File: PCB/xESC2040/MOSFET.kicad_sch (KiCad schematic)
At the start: 9 parts, among them J11 Conn_02x02_Counter_Clockwise, Q5 BSC026N08NS5, Q6 BSC026N08NS5

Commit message: WIP new power stage
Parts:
- removed C43: 1nF/100V, Capacitor_SMD:C_0603_1608Metric, symbol Device:C
- removed R43: 33mR, Resistor_SMD:R_2512_6332Metric, symbol Device:R
- removed R44: 10R, Resistor_SMD:R_0603_1608Metric, symbol Device:R
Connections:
- net DRV: now also J11.1 (Pin_1), J11.2 (Pin_2), J11.3 (Pin_3), J11.4 (Pin_4)
- net GND: no longer Q6.1 (S), Q6.2 (S), Q6.3 (S)
- new net MOSFET_GND: Q6.1 (S), Q6.2 (S), Q6.3 (S)
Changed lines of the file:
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@@
   (junction (at 231.14 83.82) (diameter 0) (color 0 0 0 0)
   )
-  (junction (at 218.44 83.82) (diameter 0) (color 0 0 0 0)
-  )
   (junction (at 243.84 86.36) (diameter 0) (color 0 0 0 0)
   )
   (junction (at 176.53 53.34) (diameter 0) (color 0 0 0 0)
   )
-  (junction (at 205.74 83.82) (diameter 0) (color 0 0 0 0)
-  )
   (wire (pts (xy 231.14 83.82) (xy 231.14 86.36))
     (stroke (width 0) (type default) (color 0 0 0 0))
@@
     (stroke (width 0) (type default) (color 0 0 0 0))
   )
-  (wire (pts (xy 218.44 97.79) (xy 218.44 83.82))
-    (stroke (width 0) (type default) (color 0 0 0 0))
-  )
   (wire (pts (xy 190.5 53.34) (xy 176.53 53.34))
     (stroke (width 0) (type default) (color 0 0 0 0))
@@
     (stroke (width 0) (type default) (color 0 0 0 0))
   )
-  (wire (pts (xy 205.74 105.41) (xy 205.74 111.76))
-    (stroke (width 0) (type default) (color 0 0 0 0))
-  )
   (wire (pts (xy 176.53 115.57) (xy 176.53 101.6))
     (stroke (width 0) (type default) (color 0 0 0 0))
@@
     (stroke (width 0) (type default) (color 0 0 0 0))
   )
-  (wire (pts (xy 218.44 105.41) (xy 218.44 115.57))
-    (stroke (width 0) (type default) (color 0 0 0 0))
-  )
   (wire (pts (xy 176.53 83.82) (xy 176.53 91.44))
     (stroke (width 0) (type default) (color 0 0 0 0))
@@
     (stroke (width 0) (type default) (color 0 0 0 0))
   )
-  (wire (pts (xy 205.74 83.82) (xy 218.44 83.82))
-    (stroke (width 0) (type default) (color 0 0 0 0))
-  )
-  (wire (pts (xy 218.44 83.82) (xy 231.14 83.82))
-    (stroke (width 0) (type default) (color 0 0 0 0))
-  )
-  (wire (pts (xy 191.77 83.82) (xy 176.53 83.82))
+  (wire (pts (xy 176.53 83.82) (xy 231.14 83.82))
     (stroke (width 0) (type default) (color 0 0 0 0))
   )
@@
     (stroke (width 0) (type default) (color 0 0 0 0))
   )
-  (wire (pts (xy 205.74 83.82) (xy 205.74 97.79))
-    (stroke (width 0) (type default) (color 0 0 0 0))
-  )
-  (wire (pts (xy 199.39 83.82) (xy 205.74 83.82))
-    (stroke (width 0) (type default) (color 0 0 0 0))
-  )
   (wire (pts (xy 168.91 71.12) (xy 157.48 71.12))
     (stroke (width 0) (type default) (color 0 0 0 0))
   )
+  (hierarchical_label "MOSFET_GND" (shape output) (at 176.53 115.57 270)
+    (effects (font (size 1.27 1.27)) (justify right))
+  )
   (hierarchical_label "DRV" (shape output) (at 135.89 83.82 180)
     (effects (font (size 1.27 1.27)) (justify right))
@@
   )
   (hierarchical_label "LS" (shape input) (at 135.89 96.52 180)
-    (effects (font (size 1.27 1.27)) (justify right))
-  )
-  (hierarchical_label "SENSE" (shape output) (at 205.74 111.76 180)
     (effects (font (size 1.27 1.27)) (justify right))
   )
@@
     (pin "5")
   )
-  (symbol (lib_id "Device:R") (at 195.58 83.82 270)
-    (in_bom yes) (on_board yes)
-    (property "Reference" "R43" (id 0) (at 195.58 78.5622 90))
-    (property "Value" "33mR" (id 1) (at 195.58 80.8736 90))
-    (property "Footprint" "Resistor_SMD:R_2512_6332Metric" (id 2) (at 195.58 82.042 90)
-      (effects (font (size 1.27 1.27)) hide)
-    )
-    (property "Datasheet" "~" (id 3) (at 195.58 83.82 0)
-      (effects (font (size 1.27 1.27)) hide)
-    )
-    (property "LCSC" "C2889925" (id 4) (at 195.58 83.82 0)
-      (effects (font (size 1.27 1.27)) hide)
-    )
-    (property "Stock_PN" "R-2512-.033-3W-5%" (id 5) (at 195.58 83.82 0)
-      (effects (font (size 1.27 1.27)) hide)
-    )
-    (pin "1")
-    (pin "2")
-  )
   (symbol (lib_id "Device:R") (at 153.67 71.12 270)
     (in_bom yes) (on_board yes)
@@
     (pin "2")
   )
-  (symbol (lib_id "Device:R") (at 205.74 101.6 0)
-    (in_bom yes) (on_board yes)
-    (property "Reference" "R44" (id 0) (at 207.518 100.4316 0)
-      (effects (font (size 1.27 1.27)) (justify left))
-    )
-    (property "Value" "10R" (id 1) (at 207.518 102.743 0)
-      (effects (font (size 1.27 1.27)) (justify left))
-    )
-    (property "Footprint" "Resistor_SMD:R_0603_1608Metric" (id 2) (at 203.962 101.6 90)
-      (effects (font (size 1.27 1.27)) hide)
-    )
-    (property "Datasheet" "~" (id 3) (at 205.74 101.6 0)
-      (effects (font (size 1.27 1.27)) hide)
-    )
-    (property "Digikey" "RMCF0603FT10R0CT-ND" (id 4) (at 205.74 101.6 0)
-      (effects (font (size 1.27 1.27)) hide)
-    )
-    (property "Part Number" "RMCF0603FT10R0" (id 5) (at 205.74 101.6 0)
-      (effects (font (size 1.27 1.27)) hide)
-    )
-    (property "Stock_PN" "R-603-10-.1W-1%" (id 6) (at 205.74 101.6 0)
-      (effects (font (size 1.27 1.27)) hide)
-    )
-    (pin "1")
-    (pin "2")
-  )
-  (symbol (lib_id "power:GND") (at 176.53 115.57 0)
-    (in_bom yes) (on_board yes)
-    (property "Reference" "#PWR042" (id 0) (at 176.53 121.92 0)
-      (effects (font (size 1.27 1.27)) hide)
-    )
-    (property "Value" "GND" (id 1) (at 176.657 119.9642 0))
-    (property "Footprint" "" (id 2) (at 176.53 115.57 0)
-      (effects (font (size 1.27 1.27)) hide)
-    )
-    (property "Datasheet" "" (id 3) (at 176.53 115.57 0)
-      (effects (font (size 1.27 1.27)) hide)
-    )
-    (pin "1")
-  )
   (symbol (lib_id "Device:C") (at 190.5 58.42 0)
     (in_bom yes) (on_board yes)
@@
       (effects (font (size 1.27 1.27)) hide)
     )
-    (pin "1")
-  )
-  (symbol (lib_id "Device:C") (at 218.44 101.6 0)
-    (in_bom yes) (on_board yes)
-    (property "Reference" "C43" (id 0) (at 221.361 100.4316 0)
-      (effects (font (size 1.27 1.27)) (justify left))
-    )
-    (property "Value" "1nF/100V" (id 1) (at 221.361 102.743 0)
-      (effects (font (size 1.27 1.27)) (justify left))
-    )
-    (property "Footprint" "Capacitor_SMD:C_0603_1608Metric" (id 2) (at 219.4052 105.41 0)
-      (effects (font (size 1.27 1.27)) hide)
-    )
-    (property "Datasheet" "~" (id 3) (at 218.44 101.6 0)
-      (effects (font (size 1.27 1.27)) hide)
-    )
-    (property "Digikey" "C-603-1000pF-100V-X7R" (id 4) (at 218.44 101.6 0)
-      (effects (font (size 1.27 1.27)) hide)
-    )
-    (property "Part Number" "490-4764-2-ND" (id 5) (at 218.44 101.6 0)
-      (effects (font (size 1.27 1.27)) hide)
-    )
-    (property "Stock_PN" "C-603-1000pF-100V-X7R" (id 6) (at 218.44 101.6 0)
-      (effects (font (size 1.27 1.27)) hide)
-    )
-    (pin "1")
-    (pin "2")
-  )
-  (symbol (lib_id "power:GND") (at 218.44 115.57 0)
-    (in_bom yes) (on_board yes)
-    (property "Reference" "#PWR044" (id 0) (at 218.44 121.92 0)
-      (effects (font (size 1.27 1.27)) hide)
-    )
-    (property "Value" "GND" (id 1) (at 218.567 119.9642 0))
-    (property "Footprint" "" (id 2) (at 218.44 115.57 0)
-      (effects (font (size 1.27 1.27)) hide)
-    )
-    (property "Datasheet" "" (id 3) (at 218.44 115.57 0)
-      (effects (font (size 1.27 1.27)) hide)
-    )

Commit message: Added some part numbers and such for the BoM.
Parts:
- Q5, Q6: Part Number BSC026N08NS5 -> C919592
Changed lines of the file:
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@@
       (effects (font (size 1.27 1.27)) (justify left) hide)
     )
-    (property "Part Number" "BSC026N08NS5" (id 4) (at 173.99 71.12 0)
+    (property "Part Number" "C919592" (id 4) (at 173.99 71.12 0)
       (effects (font (size 1.27 1.27)) hide)
     )
@@
       (effects (font (size 1.27 1.27)) (justify left) hide)
     )
-    (property "Part Number" "BSC026N08NS5" (id 4) (at 173.99 96.52 0)
+    (property "Part Number" "C919592" (id 4) (at 173.99 96.52 0)
       (effects (font (size 1.27 1.27)) hide)
     )

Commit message: add pn's for header pins - all cheapies from LSCS
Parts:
- J11: LCSC (none) -> C124362; Part Number (none) -> B-2100S04P-B110; Stock_PN (none) -> J-TH-2x2-.1
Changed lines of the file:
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@@
+      (effects (font (size 1.27 1.27)) hide)
+    )
+    (property "LCSC" "C124362" (id 4) (at 236.22 83.82 0)
+      (effects (font (size 1.27 1.27)) hide)
+    )
+    (property "Part Number" "B-2100S04P-B110" (id 5) (at 236.22 83.82 0)
+      (effects (font (size 1.27 1.27)) hide)
+    )
+    (property "Stock_PN" "J-TH-2x2-.1" (id 6) (at 236.22 83.82 0)
       (effects (font (size 1.27 1.27)) hide)
     )

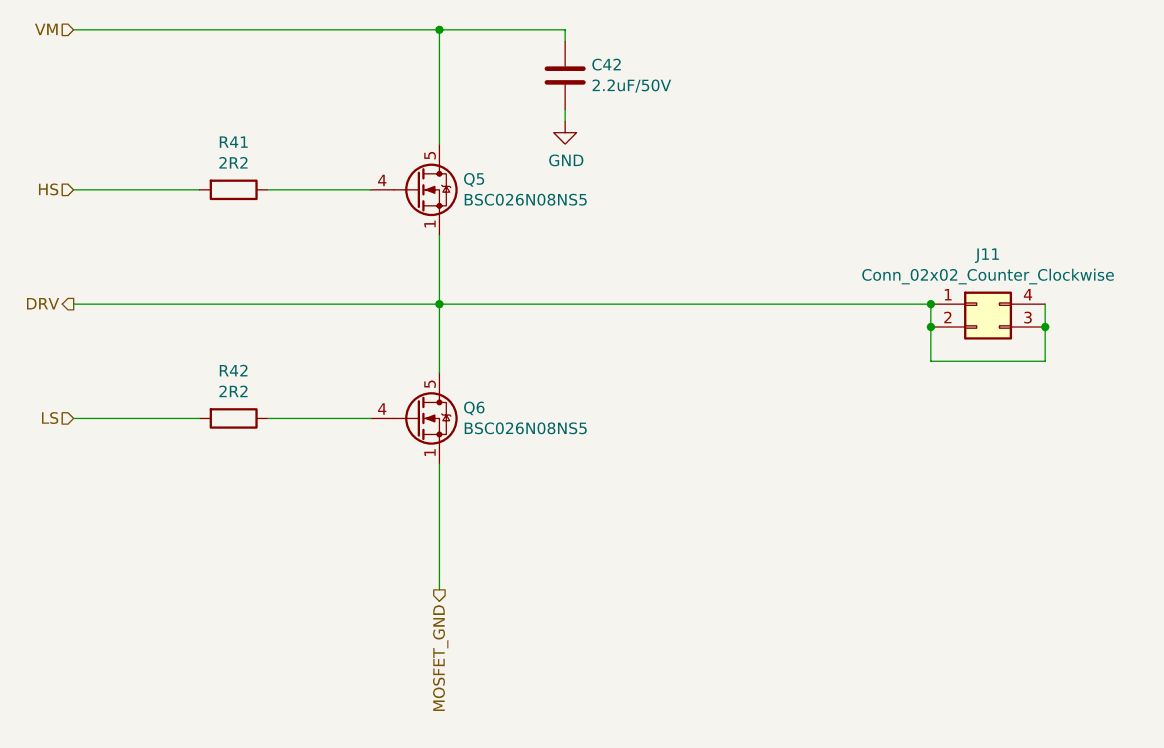
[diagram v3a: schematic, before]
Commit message: Merge J5 and J1 into one connector - no pinout changes or connector move
With J5 gone had kicad redo  reference designators - hope that's ok
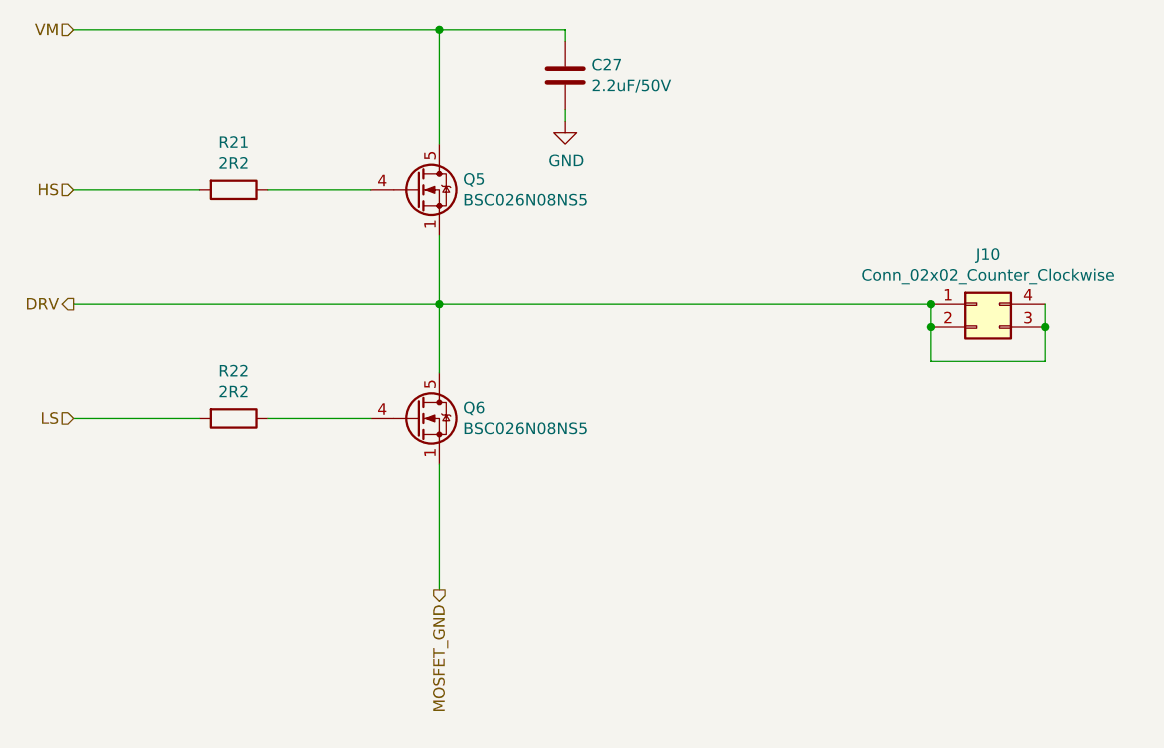
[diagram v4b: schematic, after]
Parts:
- renumbered C42 to C27, J11 to J10, R41 to R21, R42 to R22
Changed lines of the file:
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@@
   (symbol (lib_id "Device:R") (at 153.67 71.12 270)
     (in_bom yes) (on_board yes)
-    (property "Reference" "R41" (id 0) (at 153.67 65.8622 90))
+    (property "Reference" "R21" (id 0) (at 153.67 65.8622 90))
     (property "Value" "2R2" (id 1) (at 153.67 68.1736 90))
     (property "Footprint" "Resistor_SMD:R_0603_1608Metric" (id 2) (at 153.67 69.342 90)
@@
   (symbol (lib_id "Device:R") (at 153.67 96.52 270)
     (in_bom yes) (on_board yes)
-    (property "Reference" "R42" (id 0) (at 153.67 91.2622 90))
+    (property "Reference" "R22" (id 0) (at 153.67 91.2622 90))
     (property "Value" "2R2" (id 1) (at 153.67 93.5736 90))
     (property "Footprint" "Resistor_SMD:R_0603_1608Metric" (id 2) (at 153.67 94.742 90)
@@
   (symbol (lib_id "Device:C") (at 190.5 58.42 0)
     (in_bom yes) (on_board yes)
-    (property "Reference" "C42" (id 0) (at 193.421 57.2516 0)
+    (property "Reference" "C27" (id 0) (at 193.421 57.2516 0)
       (effects (font (size 1.27 1.27)) (justify left))
     )
@@
   (symbol (lib_id "power:GND") (at 190.5 63.5 0)
     (in_bom yes) (on_board yes)
-    (property "Reference" "#PWR043" (id 0) (at 190.5 69.85 0)
+    (property "Reference" "#PWR037" (id 0) (at 190.5 69.85 0)
       (effects (font (size 1.27 1.27)) hide)
     )
@@
   (symbol (lib_id "Connector_Generic:Conn_02x02_Counter_Clockwise") (at 236.22 83.82 0)
     (in_bom yes) (on_board yes)
-    (property "Reference" "J11" (id 0) (at 237.49 78.3082 0))
+    (property "Reference" "J10" (id 0) (at 237.49 78.3082 0))
     (property "Value" "Conn_02x02_Counter_Clockwise" (id 1) (at 237.49 80.6196 0))
     (property "Footprint" "Connector_PinHeader_2.54mm:PinHeader_2x02_P2.54mm_Vertical" (id 2) (at 236.22 83.82 0)

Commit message: BoM data updates
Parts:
- R21, R22: Digikey ERJ-3GEYJ2R2V -> P2.2GCT-ND; Part Number P2.2GCT-ND -> ERJ-3GEYJ2R2V
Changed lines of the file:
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@@
       (effects (font (size 1.27 1.27)) hide)
     )
-    (property "Digikey" "ERJ-3GEYJ2R2V" (id 4) (at 153.67 71.12 0)
+    (property "Digikey" "P2.2GCT-ND" (id 4) (at 153.67 71.12 0)
       (effects (font (size 1.27 1.27)) hide)
     )
-    (property "Part Number" "P2.2GCT-ND" (id 5) (at 153.67 71.12 0)
+    (property "Part Number" "ERJ-3GEYJ2R2V" (id 5) (at 153.67 71.12 0)
       (effects (font (size 1.27 1.27)) hide)
     )
@@
       (effects (font (size 1.27 1.27)) hide)
     )
-    (property "Digikey" "ERJ-3GEYJ2R2V" (id 4) (at 153.67 96.52 0)
+    (property "Digikey" "P2.2GCT-ND" (id 4) (at 153.67 96.52 0)
       (effects (font (size 1.27 1.27)) hide)
     )
-    (property "Part Number" "P2.2GCT-ND" (id 5) (at 153.67 96.52 0)
+    (property "Part Number" "ERJ-3GEYJ2R2V" (id 5) (at 153.67 96.52 0)
       (effects (font (size 1.27 1.27)) hide)
     )

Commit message: wip
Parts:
- renumbered C27 to C18, J10 to J6, Q5 to Q1, Q6 to Q2, R21 to R15, R22 to R16
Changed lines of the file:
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@@
     (effects (font (size 1.27 1.27)) (justify right))
   )
-  (symbol (lib_id "Transistor_FET:BSC026N08NS5") (at 173.99 71.12 0)
+  (symbol (lib_id "Transistor_FET:BSC026N08NS5") (at 173.99 71.12 0) (unit 1)
     (in_bom yes) (on_board yes)
-    (property "Reference" "Q5" (id 0) (at 179.1716 69.9516 0)
+    (property "Reference" "Q1" (id 0) (at 179.1716 69.9516 0)
       (effects (font (size 1.27 1.27)) (justify left))
     )
@@
     (pin "5")
   )
-  (symbol (lib_id "Transistor_FET:BSC026N08NS5") (at 173.99 96.52 0)
+  (symbol (lib_id "Transistor_FET:BSC026N08NS5") (at 173.99 96.52 0) (unit 1)
     (in_bom yes) (on_board yes)
-    (property "Reference" "Q6" (id 0) (at 179.1716 95.3516 0)
+    (property "Reference" "Q2" (id 0) (at 179.1716 95.3516 0)
       (effects (font (size 1.27 1.27)) (justify left))
     )
@@
     (pin "5")
   )
-  (symbol (lib_id "Device:R") (at 153.67 71.12 270)
+  (symbol (lib_id "Device:R") (at 153.67 71.12 270) (unit 1)
     (in_bom yes) (on_board yes)
-    (property "Reference" "R21" (id 0) (at 153.67 65.8622 90))
+    (property "Reference" "R15" (id 0) (at 153.67 65.8622 90))
     (property "Value" "2R2" (id 1) (at 153.67 68.1736 90))
     (property "Footprint" "Resistor_SMD:R_0603_1608Metric" (id 2) (at 153.67 69.342 90)
@@
     (pin "2")
   )
-  (symbol (lib_id "Device:R") (at 153.67 96.52 270)
+  (symbol (lib_id "Device:R") (at 153.67 96.52 270) (unit 1)
     (in_bom yes) (on_board yes)
-    (property "Reference" "R22" (id 0) (at 153.67 91.2622 90))
+    (property "Reference" "R16" (id 0) (at 153.67 91.2622 90))
     (property "Value" "2R2" (id 1) (at 153.67 93.5736 90))
     (property "Footprint" "Resistor_SMD:R_0603_1608Metric" (id 2) (at 153.67 94.742 90)
@@
     (pin "2")
   )
-  (symbol (lib_id "Device:C") (at 190.5 58.42 0)
+  (symbol (lib_id "Device:C") (at 190.5 58.42 0) (unit 1)
     (in_bom yes) (on_board yes)
-    (property "Reference" "C27" (id 0) (at 193.421 57.2516 0)
+    (property "Reference" "C18" (id 0) (at 193.421 57.2516 0)
       (effects (font (size 1.27 1.27)) (justify left))
     )
@@
     (pin "2")
   )
-  (symbol (lib_id "power:GND") (at 190.5 63.5 0)
+  (symbol (lib_id "power:GND") (at 190.5 63.5 0) (unit 1)
     (in_bom yes) (on_board yes)
-    (property "Reference" "#PWR037" (id 0) (at 190.5 69.85 0)
+    (property "Reference" "#PWR022" (id 0) (at 190.5 69.85 0)
       (effects (font (size 1.27 1.27)) hide)
     )
@@
     (pin "1")
   )
-  (symbol (lib_id "Connector_Generic:Conn_02x02_Counter_Clockwise") (at 236.22 83.82 0)
+  (symbol (lib_id "Connector_Generic:Conn_02x02_Counter_Clockwise") (at 236.22 83.82 0) (unit 1)
     (in_bom yes) (on_board yes)
-    (property "Reference" "J10" (id 0) (at 237.49 78.3082 0))
+    (property "Reference" "J6" (id 0) (at 237.49 78.3082 0))
     (property "Value" "Conn_02x02_Counter_Clockwise" (id 1) (at 237.49 80.6196 0))
     (property "Footprint" "Connector_PinHeader_2.54mm:PinHeader_2x02_P2.54mm_Vertical" (id 2) (at 236.22 83.82 0)
